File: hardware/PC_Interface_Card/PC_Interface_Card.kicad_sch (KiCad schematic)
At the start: 79 parts, among them J1 GSB1C41110SSHR, J2 DM3BT-DSF-PEJS, J3 BM11B-GHS-TBT, J4 GHR-11V-S, J5 GHR-11V-S, SW1 CherryMX, SW2 CherryMX, SW3 CherryMX, SW4 CherryMX, SW5 CherryMX, SW6 TL1240YQ2JBLK, SW7 TL1240YQ2JBLK, SW8 TL1240YQ2JBLK, U1 USBLC6-2SC6, U2 TLV1117LV33DCYR, U3 MB85RS4MTYPN-GS-AWEWE1, U4 ESP32-S3-WROOM-1

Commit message: Start of day work - 24/01
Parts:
- added H1, H10, H2, H3, H4, H5, H6, H7, H8, H9: MountingHole_Pad, MountingHole:MountingHole_2.2mm_M2_Pad_Via, symbol Mechanical:MountingHole_Pad
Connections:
- net GND: now also H1.1, H10.1, H2.1, H3.1, H4.1, H5.1, H6.1, H7.1, H8.1, H9.1
- net VCC renamed 3V3
- net 3V3: no longer R13.2, R18.2, R20.2
- net VLDO renamed VLDO_In
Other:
- note added: "Mounting Holes"
- moved on the sheet: C10, C11, C12, C5, C6, C7, C8, C9, J4, J5, LED1, LED2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

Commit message: Alignment of moounting holes and final layout
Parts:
- removed H3, H8: MountingHole_Pad, MountingHole:MountingHole_2.2mm_M2_Pad_Via, symbol Mechanical:MountingHole_Pad
- renumbered H7 to H3, H9 to H5, H5 to H6, H10 to H7, H6 to H8, J4 to J3, J3 to J4, R12 to R10, R13 to R11, R16 to R12, R14 to R13, R15 to R14, R18 to R15, R20 to R16, R19 to R18, R21 to R19, R22 to R20, R24 to R21, R25 to R22, R27 to R24, R26 to R25, R28 to R26, R29 to R27, R30 to R28, R33 to R29, R34 to R30, R10 to R8, R11 to R9
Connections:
- net 3V3: now also R11.2, R15.2, R16.2

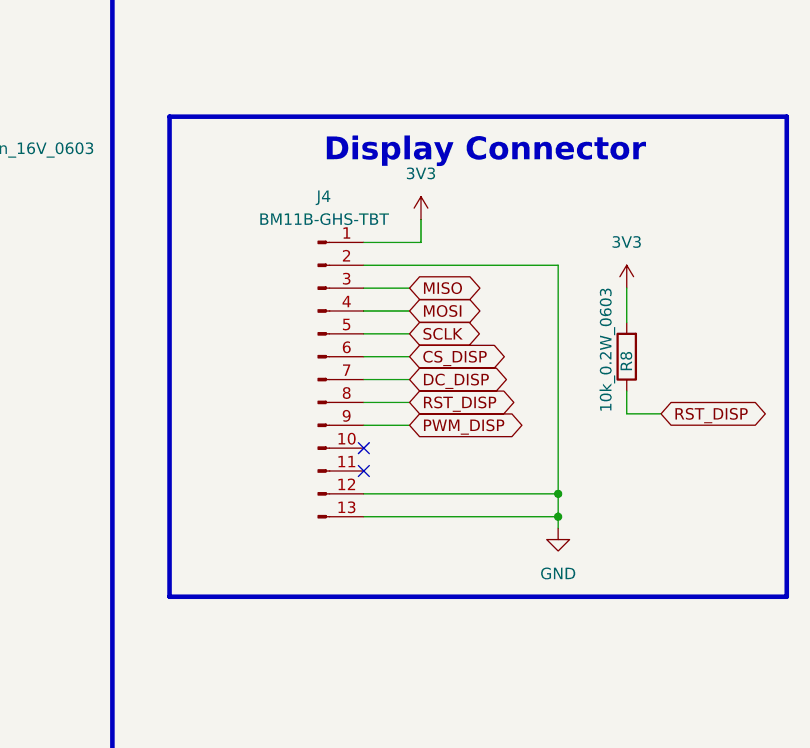
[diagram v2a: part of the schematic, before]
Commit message: More alyout work, added DRC Error output for 26012026
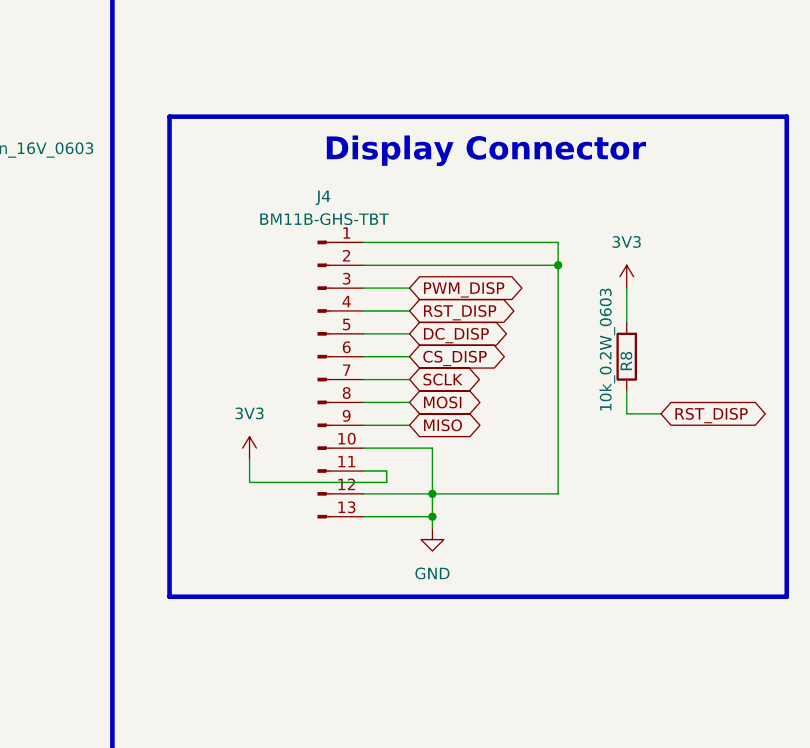
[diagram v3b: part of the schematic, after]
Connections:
- net 3V3: now also J4.11 (Pin_11); no longer J4.1 (Pin_1)
- net DC_DISP: now also J4.5 (Pin_5); no longer J4.7 (Pin_7)
- net GND: now also J4.1 (Pin_1), J4.10 (Pin_10)
- net MISO: now also J4.9 (Pin_9); no longer J4.3 (Pin_3)
- net MOSI: now also J4.8 (Pin_8); no longer J4.4 (Pin_4)
- net PWM_DISP: now also J4.3 (Pin_3); no longer J4.9 (Pin_9)
- net RST_DISP: now also J4.4 (Pin_4); no longer J4.8 (Pin_8)
- net SCLK: now also J4.7 (Pin_7); no longer J4.5 (Pin_5)
- no-connect marks 15 -> 13

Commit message: layout changes
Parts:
- removed R28, R30: 68R_0.2W_0603, Resistor_SMD:R_0603_1608Metric, symbol Device:R
- removed SW7, SW8: TL1240YQ2JBLK, Footprint:TL1240YQ, symbol Custom_Switch_LED:TL1240YQ2JBLK
- added SW7, SW8: SW_Push, Button_Switch_THT:SW_PUSH_6mm, symbol Switch:SW_Push
- U4: footprint RF_Module:ESP32-S3-WROOM-1 -> RF_Module:ESP32-S3-WROOM-1U
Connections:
- net CLK_SDMMC: now also U4.8 (IO15); no longer U4.32 (IO39)
- net CMD_SDMMC: now also U4.7 (IO7); no longer U4.31 (IO38)
- net D0_SDMMC: now also U4.9 (IO16); no longer U4.33 (IO40)
- net D1_SDMMC: now also U4.10 (IO17); no longer U4.34 (IO41)
- net D2_SDMMC: now also U4.11 (IO18); no longer U4.35 (IO42)
- net ENC_A: now also U4.37 (TXD0); no longer U4.4 (IO4)
- net ENC_B: now also U4.36 (RXD0); no longer U4.5 (IO5)
- net ENC_SW: now also U4.35 (IO42); no longer U4.6 (IO6)
- net FRAM_CS: now also U4.12 (IO8); no longer U4.22 (IO14)
- net GND: now also SW7.2, SW8.2
- net RST_DISP: now also U4.22 (IO14); no longer U4.12 (IO8)
- net SW_BOOT: now also SW7.1
- net SW_DN: now also U4.34 (IO41); no longer U4.11 (IO18)
- net SW_EN: now also SW8.1
- net SW_LEFT: now also U4.33 (IO40); no longer U4.10 (IO17)
- net SW_MENU: now also U4.5 (IO5); no longer U4.8 (IO15)
- net SW_PLAY: now also U4.32 (IO39); no longer U4.36 (RXD0)
- net SW_RIGHT: now also U4.31 (IO38); no longer U4.37 (TXD0)
- net SW_UP: now also U4.6 (IO6); no longer U4.9 (IO16)
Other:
- moved on the sheet: C17, C19, R27, R29

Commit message: Some DRC errors remain - clarifications on Monday then fab
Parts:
- removed H3, H4, H5, H8: MountingHole_Pad, MountingHole:MountingHole_2.2mm_M2_Pad_Via, symbol Mechanical:MountingHole_Pad
- added R28: 10k_0.2W_0603, Resistor_SMD:R_0603_1608Metric, symbol Device:R
- added R30, R33, R34, R35: 0R_0.1W_0603, Resistor_SMD:R_0603_1608Metric, symbol Device:R
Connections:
- net 3V3: now also R21.2, R28.2, R30.1, R33.2, R34.2, R35.1; no longer C1.1, C13.1, C15.1, C16.1, C18.1, C2.1, J2.4 (VDD), J4.11 (Pin_11), U3.8 (VDD), U4.2 (3V3)
- net CLK_SDMMC: now also U4.4 (IO4); no longer U4.8 (IO15)
- net CMD_SDMMC: now also U4.5 (IO5); no longer U4.7 (IO7)
- net CS_DISP: now also U4.10 (IO17); no longer U4.18 (IO10)
- net D0_SDMMC: now also U4.8 (IO15); no longer U4.9 (IO16)
- net D1_SDMMC: now also U4.9 (IO16); no longer U4.10 (IO17)
- net D2_SDMMC: now also U4.7 (IO7); no longer U4.11 (IO18)
- net D3_SDMMC: now also U4.6 (IO6); no longer U4.24 (IO47)
- net DC_DISP: now also U4.11 (IO18); no longer U4.17 (IO9)
- net ENC_A: now also U4.24 (IO47); no longer U4.37 (TXD0)
- net ENC_B: now also U4.23 (IO21); no longer U4.36 (RXD0)
- net FRAM_CS: now also U4.18 (IO10), R28.1; no longer U4.12 (IO8)
- net GND: no longer R21.1
- net PWM_DISP: now also U4.17 (IO9); no longer U4.25 (IO48)
- net RST_DISP: now also U4.12 (IO8); no longer U4.22 (IO14)
- net SW_MENU: now also U4.22 (IO14); no longer U4.5 (IO5)
- net SW_UP: now also U4.25 (IO48); no longer U4.6 (IO6)
- net at U3.7 (*RESET): now also R21.1; no longer R21.2
- new net: C16.1, C18.1, R30.2, U4.2 (3V3)
- new net: C13.1, C15.1, R33.1, U3.8 (VDD)
- new net: C1.1, C2.1, J2.4 (VDD), R34.1
- new net: J4.11 (Pin_11), R35.2
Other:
- moved on the sheet: H6, H7, R21

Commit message: MkII ready to fab but SMD via error still coming on JLCPCB gerber viewer - need to figure out why and close
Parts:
- C1, C13, C16, C3: value 1u_16V_0603 -> 1u_50V_0603; LCSC (none) -> C15849
- C10, C11, C12, C14, C15, C17, C18, C19, C2, C4, C5, C6, C7, C8, C9: value 100n_16V_0603 -> 100n_50V_0603; LCSC (none) -> C14663
- CR1: footprint Footprint_Project_PC_Interface:SS14_CR_SMA_403AE_OSI-M -> Diode_SMD:D_SMA; LCSC (none) -> C2480
- F1, FL1, J1, J2, J4, MT1, R24, SW1, SW2, SW3, SW4, SW5, SW6, SW7, SW8, U1, U2, U3: now not fitted
- R1, R10, R11, R12, R13, R14, R15, R16, R19, R2, R21, R22, R26, R27, R28, R29, R3, R31, R32, R4, R5, R8, R9: value 10k_0.2W_0603 -> 10k_0.1W_0603; LCSC (none) -> C25804
- R17, R18, R20, R23, R25: value 33R_0.2W_0603 -> 33R_0.1W_0603; LCSC (none) -> C23140
- R30, R33, R34, R35: LCSC (none) -> C21189
- R6, R7: value 5.1k_0.2W_0603 -> 5.1k_0.1W_0603; LCSC (none) -> C23186
- U4: LCSC (none) -> C2913202
